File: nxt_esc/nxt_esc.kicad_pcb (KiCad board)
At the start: 2 copper layers, 47.6 x 47.6 mm, 18 parts, among them IC1 L293D, J1 NXT_MOTOR, J2 NXT_MOTOR, SW1 Skid Steer/Drive & Steer, SW2 Center Steering, U1 LM7805CT

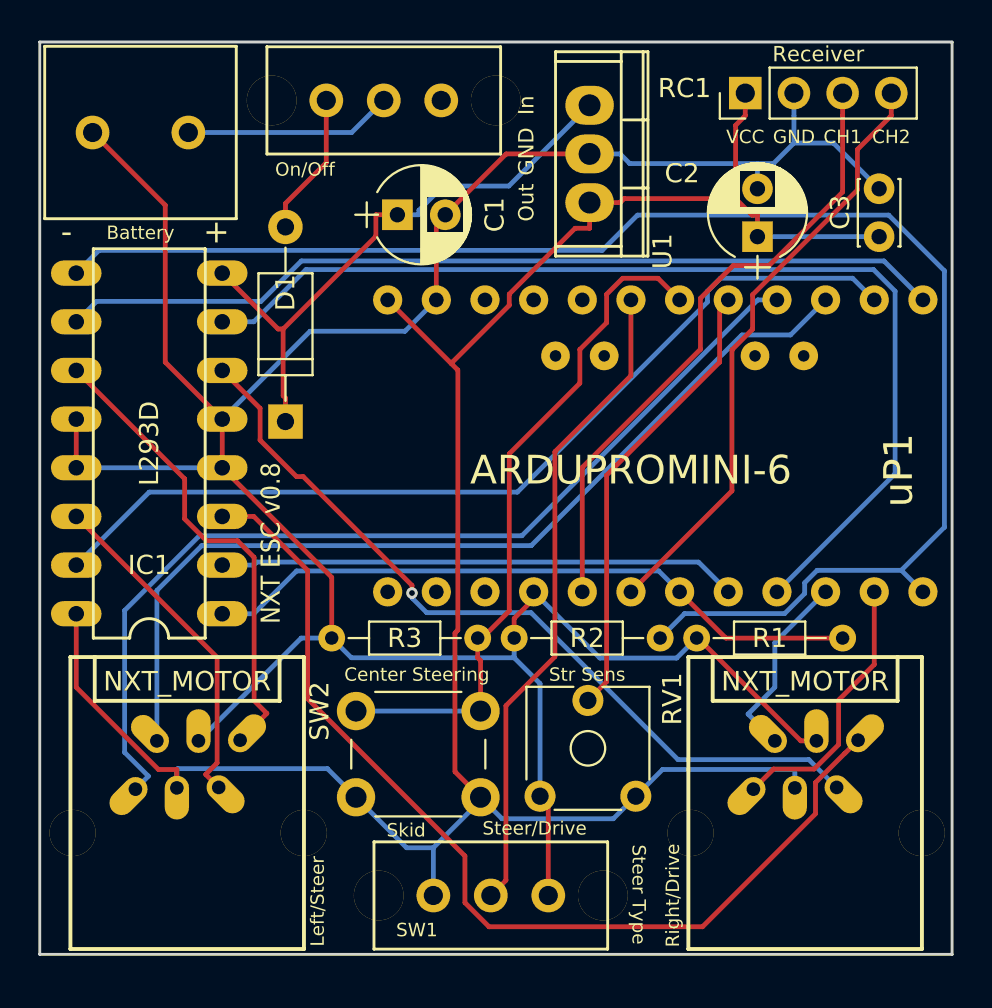
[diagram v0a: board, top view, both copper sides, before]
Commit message: Added planes for ground and power
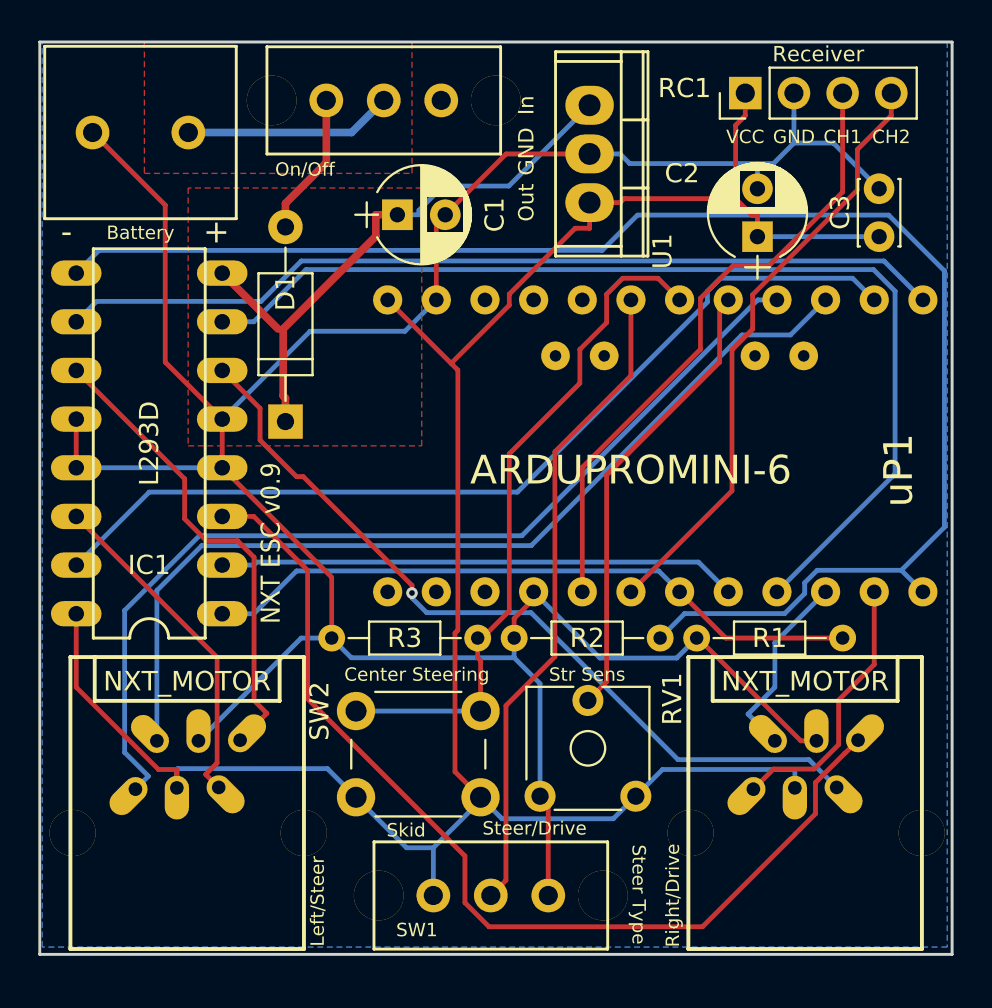
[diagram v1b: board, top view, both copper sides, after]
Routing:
- added copper zone on B.Cu, net GND
- added copper zone on F.Cu, net Net-(BT1-Pad1)
- added copper zone on F.Cu, net VCC
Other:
- board text added: "NXT ESC v0.9"
- board text removed: "NXT ESC v0.8"
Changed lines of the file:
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@@
-(kicad_pcb (version 4) (host pcbnew 4.0.7)
+(kicad_pcb (version 20171130) (host pcbnew 5.0.0-fee4fd1~66~ubuntu16.04.1)
   (general
-    (links 57)
-    (no_connects 0)
-    (area 111.049999 65.88 176.76 125.170001)
     (thickness 1.6)
     (drawings 24)
@@
     (mod_text_size 1 1)
     (mod_text_width 0.15)
-    (pad_size 1.524 1.524)
-    (pad_drill 0.762)
+    (pad_size 1.8 1.8)
+    (pad_drill 0.9)
     (pad_to_mask_clearance 0.2)
     (aux_axis_origin 0 0)
     (visible_elements 7FFFFFFF)
     (pcbplotparams
-      (layerselection 0x010f0_80000001)
+      (layerselection 0x010f0_ffffffff)
       (usegerberextensions false)
+      (usegerberattributes false)
+      (usegerberadvancedattributes false)
+      (creategerberjobfile false)
       (excludeedgelayer true)
       (linewidth 0.100000)
@@
       (hpglpennumber 1)
       (hpglpenspeed 20)
-      (hpglpendiameter 15)
-      (hpglpenoverlay 2)
+      (hpglpendiameter 15.000000)
       (psnegative false)
       (psa4output false)
@@
       (drillshape 0)
       (scaleselection 1)
-      (outputdirectory nxt_esc.gerber/))
+      (outputdirectory "nxt_esc.gerber/"))
   )
   (net 0 "")
@@
       (net 22 "Net-(R3-Pad2)"))
     (model ${KISYS3DMOD}/Buttons_Switches_THT.3dshapes/SW_PUSH_6mm.wrl
-      (at (xyz 0.005 0 0))
+      (offset (xyz 0.1269999980926514 0 0))
       (scale (xyz 0.3937 0.3937 0.3937))
       (rotate (xyz 0 0 0))
@@
     (pad "" thru_hole oval (at -5.85 0) (size 2.6 2.6) (drill oval 2.6) (layers *.Cu F.SilkS))
   )
-  (gr_text "NXT ESC v0.8" (at 123.19 103.632 90) (layer F.SilkS)
+  (gr_text "NXT ESC v0.9" (at 123.19 103.632 90) (layer F.SilkS)
     (effects (font (size 1 0.9) (thickness 0.15)))
   )
@@
   (segment (start 155.7751 100.0029) (end 155.7751 90.477) (width 0.25) (layer B.Cu) (net 3))
   (segment (start 149.606 106.172) (end 155.7751 100.0029) (width 0.25) (layer B.Cu) (net 3))
-  (segment (start 123.5655 92.4505) (end 120.65 89.535) (width 0.25) (layer F.Cu) (net 4))
+  (segment (start 123.5655 92.4505) (end 120.65 89.535) (width 0.4) (layer F.Cu) (net 4))
   (segment (start 123.8305 92.4505) (end 123.5655 92.4505) (width 0.25) (layer F.Cu) (net 4))
-  (segment (start 128.6687 87.6123) (end 123.8305 92.4505) (width 0.25) (layer F.Cu) (net 4))
-  (segment (start 128.6687 86.487) (end 128.6687 87.6123) (width 0.25) (layer F.Cu) (net 4))
-  (segment (start 123.8305 95.9352) (end 123.952 96.0567) (width 0.25) (layer F.Cu) (net 4))
-  (segment (start 123.8305 92.4505) (end 123.8305 95.9352) (width 0.25) (layer F.Cu) (net 4))
-  (segment (start 129.794 86.487) (end 128.6687 86.487) (width 0.25) (layer F.Cu) (net 4))
-  (segment (start 123.952 97.282) (end 123.952 96.0567) (width 0.25) (layer F.Cu) (net 4))
+  (segment (start 128.6687 87.6123) (end 123.8305 92.4505) (width 0.4) (layer F.Cu) (net 4))
+  (segment (start 128.6687 86.487) (end 128.6687 87.6123) (width 0.4) (layer F.Cu) (net 4))
+  (segment (start 123.8305 95.9352) (end 123.952 96.0567) (width 0.4) (layer F.Cu) (net 4))
+  (segment (start 123.8305 92.4505) (end 123.8305 95.9352) (width 0.4) (layer F.Cu) (net 4))
+  (segment (start 129.794 86.487) (end 128.6687 86.487) (width 0.4) (layer F.Cu) (net 4))
+  (segment (start 123.952 97.282) (end 123.952 96.0567) (width 0.4) (layer F.Cu) (net 4))
   (segment (start 129.794 86.487) (end 130.9193 86.487) (width 0.25) (layer B.Cu) (net 4))
   (segment (start 130.9193 86.2529) (end 130.9193 86.487) (width 0.25) (layer B.Cu) (net 4))
@@
   (segment (start 135.636 107.1678) (end 135.636 98.9636) (width 0.25) (layer F.Cu) (net 22))
   (segment (start 133.985 108.8188) (end 135.636 107.1678) (width 0.25) (layer F.Cu) (net 22))
-  (segment (start 127.4066 82.1944) (end 118.883 82.1944) (width 0.25) (layer B.Cu) (net 23))
-  (segment (start 129.083 80.518) (end 127.4066 82.1944) (width 0.25) (layer B.Cu) (net 23))
-  (segment (start 126.083 83.7657) (end 123.952 85.8967) (width 0.25) (layer F.Cu) (net 24))
-  (segment (start 126.083 80.518) (end 126.083 83.7657) (width 0.25) (layer F.Cu) (net 24))
-  (segment (start 123.952 87.122) (end 123.952 85.8967) (width 0.25) (layer F.Cu) (net 24))
+  (segment (start 127.4066 82.1944) (end 118.883 82.1944) (width 0.4) (layer B.Cu) (net 23))
+  (segment (start 129.083 80.518) (end 127.4066 82.1944) (width 0.4) (layer B.Cu) (net 23))
+  (segment (start 126.083 83.7657) (end 123.952 85.8967) (width 0.4) (layer F.Cu) (net 24))
+  (segment (start 126.083 80.518) (end 126.083 83.7657) (width 0.4) (layer F.Cu) (net 24))
+  (segment (start 123.952 87.122) (end 123.952 85.8967) (width 0.4) (layer F.Cu) (net 24))
+  (zone (net 6) (net_name GND) (layer B.Cu) (hatch edge 0.508)
+    (connect_pads (clearance 0.508))
+    (min_thickness 0.254)
+    (fill yes (arc_segments 16) (thermal_gap 0.508) (thermal_bridge_width 0.508))
+    (polygon
+      (pts
+        (xy 111.252 77.47) (xy 158.496 77.47) (xy 158.496 124.714) (xy 111.252 124.714)
+      )
+    )
+  )
+  (zone (net 4) (net_name VCC) (layer F.Cu) (hatch edge 0.508)
+    (connect_pads (clearance 0.508))
+    (min_thickness 0.254)
+    (fill yes (arc_segments 16) (thermal_gap 0.508) (thermal_bridge_width 0.508))
+    (polygon
+      (pts
+        (xy 131.064 85.09) (xy 118.872 85.09) (xy 118.872 98.552) (xy 131.064 98.552)
+      )
+    )
+  )
+  (zone (net 23) (net_name "Net-(BT1-Pad1)") (layer F.Cu) (hatch edge 0.508)
+    (connect_pads (clearance 0.508))
+    (min_thickness 0.254)
+    (fill yes (arc_segments 16) (thermal_gap 0.508) (thermal_bridge_width 0.508))
+    (polygon
+      (pts
+        (xy 130.556 77.47) (xy 116.586 77.47) (xy 116.586 84.328) (xy 130.556 84.328)
+      )
+    )
+  )
 )
